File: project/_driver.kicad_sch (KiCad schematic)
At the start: 25 parts, among them U201 74HC595, U202 ULN2803A, U203 74HC595, U204 ULN2803A

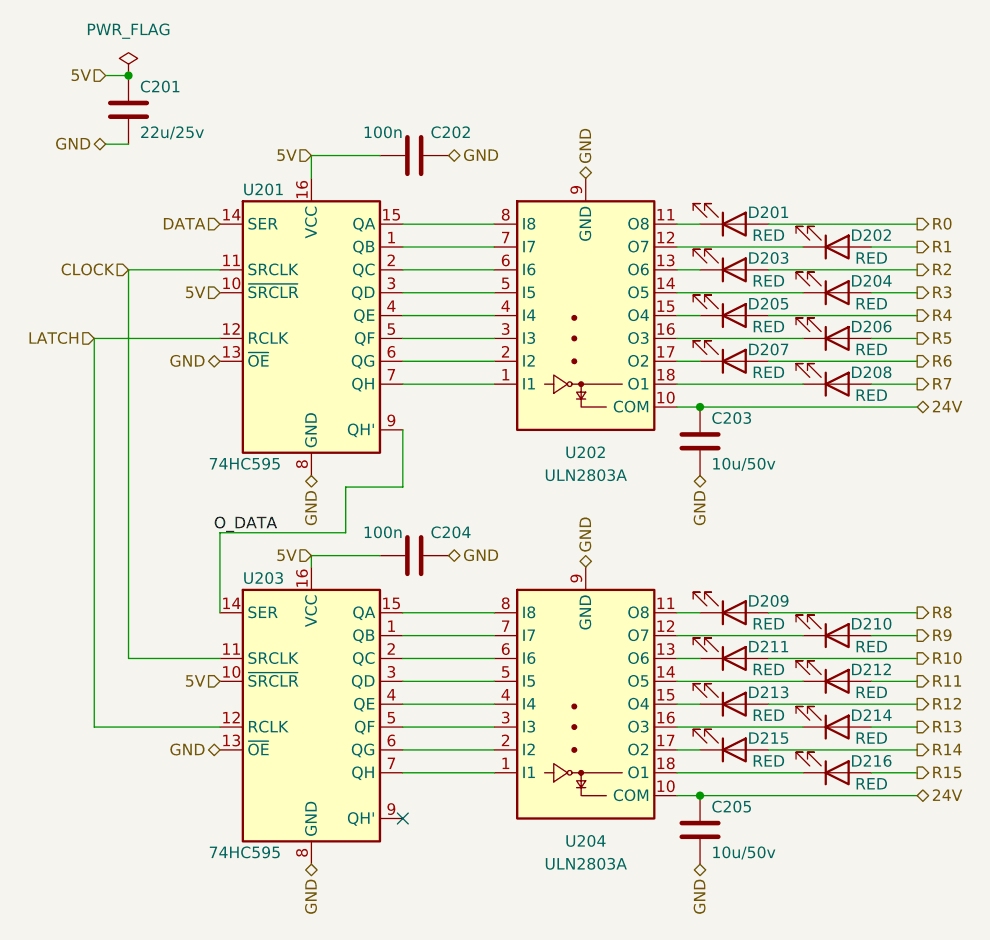
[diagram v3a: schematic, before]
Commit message: improvements for next prototype
* buck makes 6v now
* using LDO for 5v with over voltage disable
* using LDO for 3v3
* adding zener to 24v led to stop it from glowing from 5v USB
* added 0.2mm heigt for USB port hole
* both buttons now 15mm height
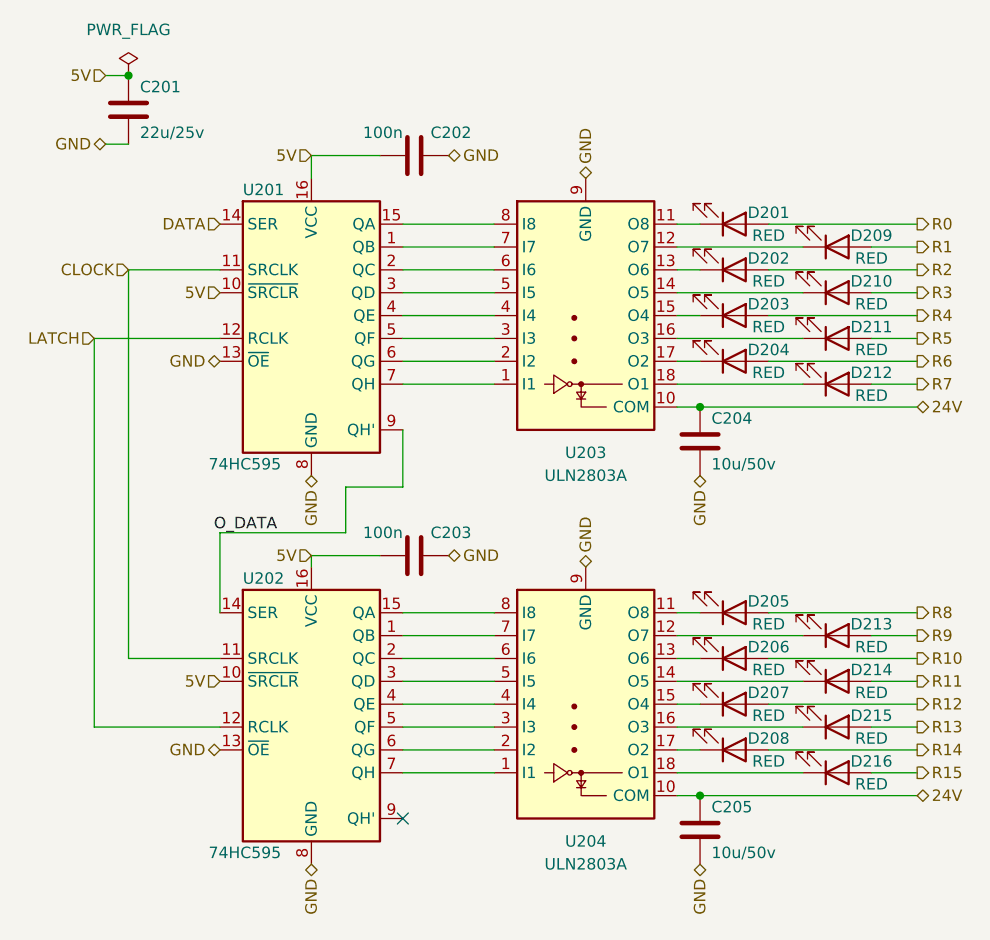
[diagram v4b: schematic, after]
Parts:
- renumbered C204 to C203, C203 to C204, D203 to D202, D205 to D203, D207 to D204, D209 to D205, D211 to D206, D213 to D207, D215 to D208, D202 to D209, D204 to D210, D206 to D211, D208 to D212, D210 to D213, D212 to D214, D214 to D215, U203 to U202, U202 to U203
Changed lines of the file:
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@@
   (symbol (lib_id "Device:LED") (at 161.29 83.82 0) (mirror x) (unit 1)
     (in_bom yes) (on_board yes)
-    (property "Reference" "D207" (id 0) (at 165.1 82.55 0))
+    (property "Reference" "D204" (id 0) (at 165.1 82.55 0))
     (property "Value" "RED" (id 1) (at 165.1 85.09 0))
     (property "Footprint" "-local:LED_1206_3216Metric_ReverseMount" (id 2) (at 161.29 83.82 0)
@@
   (symbol (lib_id "Device:LED") (at 172.72 114.3 0) (mirror x) (unit 1)
     (in_bom yes) (on_board yes)
-    (property "Reference" "D210" (id 0) (at 176.53 113.03 0))
+    (property "Reference" "D213" (id 0) (at 176.53 113.03 0))
     (property "Value" "RED" (id 1) (at 176.53 115.57 0))
     (property "Footprint" "-local:LED_1206_3216Metric_ReverseMount" (id 2) (at 172.72 114.3 0)
@@
   (symbol (lib_id "Device:C") (at 125.73 105.41 90) (unit 1)
     (in_bom yes) (on_board yes)
-    (property "Reference" "C204" (id 0) (at 132.08 102.87 90)
+    (property "Reference" "C203" (id 0) (at 132.08 102.87 90)
       (effects (font (size 1.27 1.27)) (justify left))
     )
@@
   (symbol (lib_id "Device:LED") (at 161.29 116.84 0) (mirror x) (unit 1)
     (in_bom yes) (on_board yes)
-    (property "Reference" "D211" (id 0) (at 165.1 115.57 0))
+    (property "Reference" "D206" (id 0) (at 165.1 115.57 0))
     (property "Value" "RED" (id 1) (at 165.1 118.11 0))
     (property "Footprint" "-local:LED_1206_3216Metric_ReverseMount" (id 2) (at 161.29 116.84 0)
@@
   (symbol (lib_id "Device:LED") (at 172.72 124.46 0) (mirror x) (unit 1)
     (in_bom yes) (on_board yes)
-    (property "Reference" "D214" (id 0) (at 176.53 123.19 0))
+    (property "Reference" "D215" (id 0) (at 176.53 123.19 0))
     (property "Value" "RED" (id 1) (at 176.53 125.73 0))
     (property "Footprint" "-local:LED_1206_3216Metric_ReverseMount" (id 2) (at 172.72 124.46 0)
@@
   (symbol (lib_id "Device:LED") (at 161.29 121.92 0) (mirror x) (unit 1)
     (in_bom yes) (on_board yes)
-    (property "Reference" "D213" (id 0) (at 165.1 120.65 0))
+    (property "Reference" "D207" (id 0) (at 165.1 120.65 0))
     (property "Value" "RED" (id 1) (at 165.1 123.19 0))
     (property "Footprint" "-local:LED_1206_3216Metric_ReverseMount" (id 2) (at 161.29 121.92 0)
@@
   (symbol (lib_id "Device:LED") (at 161.29 111.76 0) (mirror x) (unit 1)
     (in_bom yes) (on_board yes)
-    (property "Reference" "D209" (id 0) (at 165.1 110.49 0))
+    (property "Reference" "D205" (id 0) (at 165.1 110.49 0))
     (property "Value" "RED" (id 1) (at 165.1 113.03 0))
     (property "Footprint" "-local:LED_1206_3216Metric_ReverseMount" (id 2) (at 161.29 111.76 0)
@@
   (symbol (lib_id "Device:LED") (at 172.72 81.28 0) (mirror x) (unit 1)
     (in_bom yes) (on_board yes)
-    (property "Reference" "D206" (id 0) (at 176.53 80.01 0))
+    (property "Reference" "D211" (id 0) (at 176.53 80.01 0))
     (property "Value" "RED" (id 1) (at 176.53 82.55 0))
     (property "Footprint" "-local:LED_1206_3216Metric_ReverseMount" (id 2) (at 172.72 81.28 0)
@@
   (symbol (lib_id "Device:LED") (at 172.72 76.2 0) (mirror x) (unit 1)
     (in_bom yes) (on_board yes)
-    (property "Reference" "D204" (id 0) (at 176.53 74.93 0))
+    (property "Reference" "D210" (id 0) (at 176.53 74.93 0))
     (property "Value" "RED" (id 1) (at 176.53 77.47 0))
     (property "Footprint" "-local:LED_1206_3216Metric_ReverseMount" (id 2) (at 172.72 76.2 0)
@@
   (symbol (lib_id "Device:LED") (at 172.72 86.36 0) (mirror x) (unit 1)
     (in_bom yes) (on_board yes)
-    (property "Reference" "D208" (id 0) (at 176.53 85.09 0))
+    (property "Reference" "D212" (id 0) (at 176.53 85.09 0))
     (property "Value" "RED" (id 1) (at 176.53 87.63 0))
     (property "Footprint" "-local:LED_1206_3216Metric_ReverseMount" (id 2) (at 172.72 86.36 0)
@@
   (symbol (lib_id "74xx:74HC595") (at 114.3 121.92 0) (unit 1)
     (in_bom yes) (on_board yes)
-    (property "Reference" "U203" (id 0) (at 106.68 107.95 0)
+    (property "Reference" "U202" (id 0) (at 106.68 107.95 0)
       (effects (font (size 1.27 1.27)) (justify left))
     )
@@
   (symbol (lib_id "Device:LED") (at 172.72 119.38 0) (mirror x) (unit 1)
     (in_bom yes) (on_board yes)
-    (property "Reference" "D212" (id 0) (at 176.53 118.11 0))
+    (property "Reference" "D214" (id 0) (at 176.53 118.11 0))
     (property "Value" "RED" (id 1) (at 176.53 120.65 0))
     (property "Footprint" "-local:LED_1206_3216Metric_ReverseMount" (id 2) (at 172.72 119.38 0)
@@
   (symbol (lib_id "Device:LED") (at 161.29 78.74 0) (mirror x) (unit 1)
     (in_bom yes) (on_board yes)
-    (property "Reference" "D205" (id 0) (at 165.1 77.47 0))
+    (property "Reference" "D203" (id 0) (at 165.1 77.47 0))
     (property "Value" "RED" (id 1) (at 165.1 80.01 0))
     (property "Footprint" "-local:LED_1206_3216Metric_ReverseMount" (id 2) (at 161.29 78.74 0)
@@
   (symbol (lib_id "Device:LED") (at 161.29 73.66 0) (mirror x) (unit 1)
     (in_bom yes) (on_board yes)
-    (property "Reference" "D203" (id 0) (at 165.1 72.39 0))
+    (property "Reference" "D202" (id 0) (at 165.1 72.39 0))
     (property "Value" "RED" (id 1) (at 165.1 74.93 0))
     (property "Footprint" "-local:LED_1206_3216Metric_ReverseMount" (id 2) (at 161.29 73.66 0)
@@
   (symbol (lib_id "Device:LED") (at 172.72 71.12 0) (mirror x) (unit 1)
     (in_bom yes) (on_board yes)
-    (property "Reference" "D202" (id 0) (at 176.53 69.85 0))
+    (property "Reference" "D209" (id 0) (at 176.53 69.85 0))
     (property "Value" "RED" (id 1) (at 176.53 72.39 0))
     (property "Footprint" "-local:LED_1206_3216Metric_ReverseMount" (id 2) (at 172.72 71.12 0)
@@
   (symbol (lib_id "Device:LED") (at 161.29 127 0) (mirror x) (unit 1)
     (in_bom yes) (on_board yes)
-    (property "Reference" "D215" (id 0) (at 165.1 125.73 0))
+    (property "Reference" "D208" (id 0) (at 165.1 125.73 0))
     (property "Value" "RED" (id 1) (at 165.1 128.27 0))
     (property "Footprint" "-local:LED_1206_3216Metric_ReverseMount" (id 2) (at 161.29 127 0)
@@
   (symbol (lib_id "Device:C") (at 157.48 92.71 0) (unit 1)
     (in_bom yes) (on_board yes)
-    (property "Reference" "C203" (id 0) (at 158.75 90.17 0)
+    (property "Reference" "C204" (id 0) (at 158.75 90.17 0)
       (effects (font (size 1.27 1.27)) (justify left))
     )
@@
   (symbol (lib_id "Transistor_Array:ULN2803A") (at 144.78 81.28 0) (mirror x) (unit 1)
     (in_bom yes) (on_board yes) (fields_autoplaced)
-    (property "Reference" "U202" (id 0) (at 144.78 93.98 0))
+    (property "Reference" "U203" (id 0) (at 144.78 93.98 0))
     (property "Value" "ULN2803A" (id 1) (at 144.78 96.52 0))
     (property "Footprint" "Package_SO:SOIC-18W_7.5x11.6mm_P1.27mm" (id 2) (at 146.05 64.77 0)
